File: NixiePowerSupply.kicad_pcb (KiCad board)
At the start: 2 copper layers, 22 parts, among them J1 BARREL_JACK, J2 CONN_01X04, J3 CONN_01X05, Q1 2SA1015, Q2 2SK3234, U1 NJM2360, U2 7805

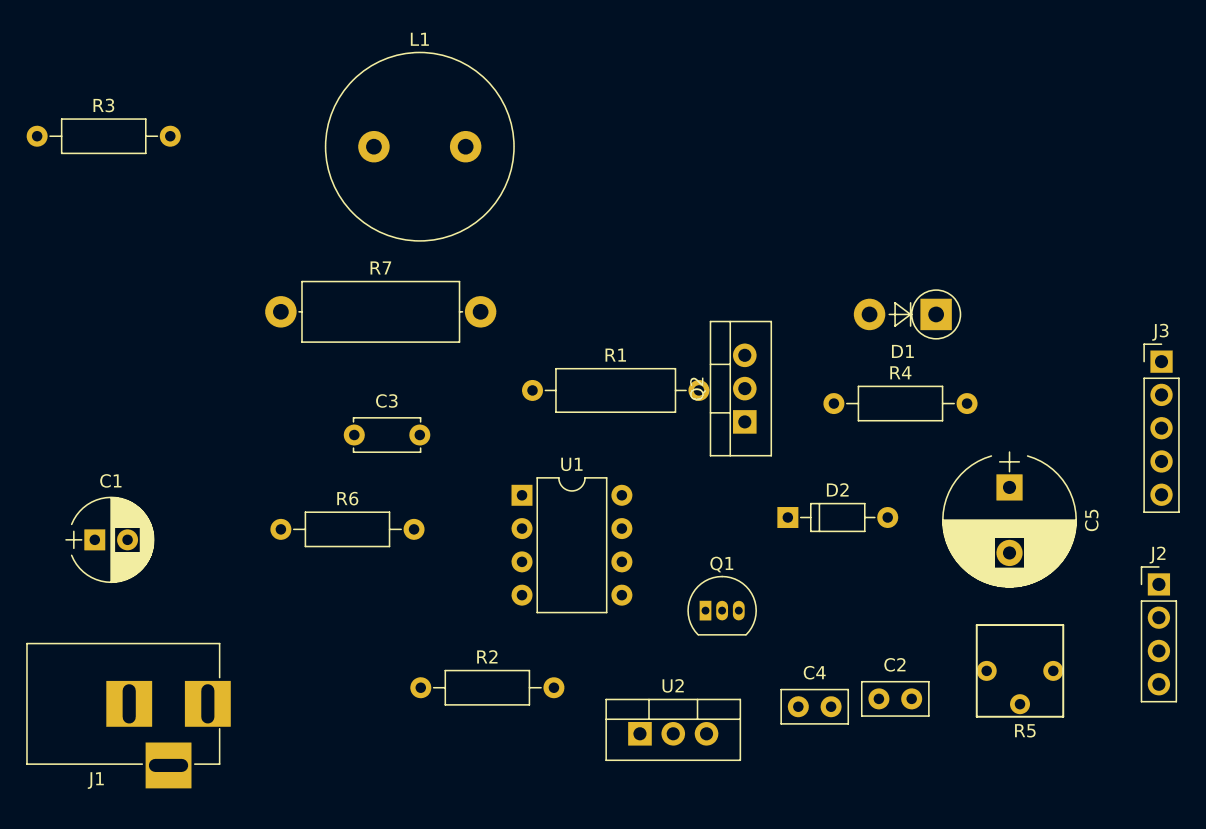
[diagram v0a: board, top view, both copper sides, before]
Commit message: parts moved for layout chnge
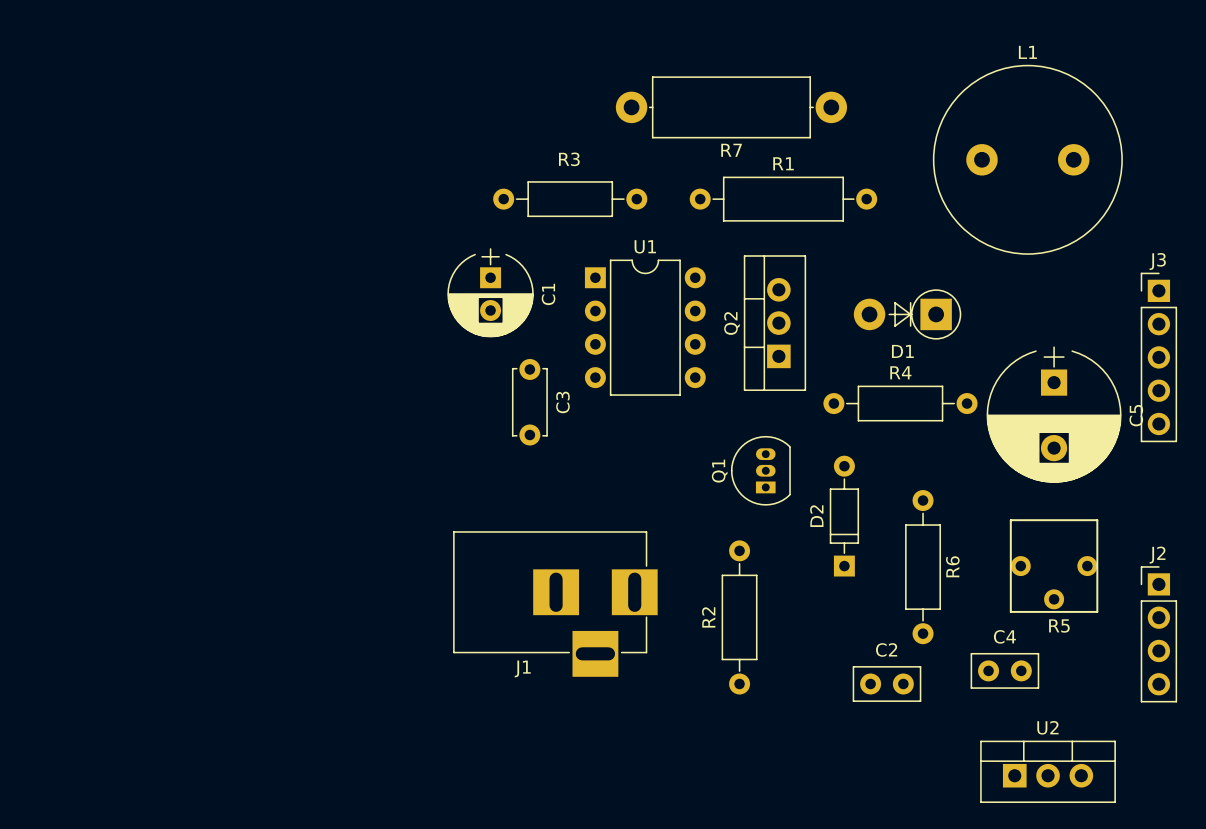
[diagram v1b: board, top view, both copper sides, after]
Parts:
- moved R6 49.0 mm to (206.0, 56.0), turned to 270 degrees
- moved L1 46.4 mm to (214.0, 30.0)
- moved R7 44.8 mm to (199.0, 26.0), turned to 180 degrees
- moved C1 36.2 mm to (173.0, 39.0), turned to 270 degrees
- moved R3 35.9 mm to (174.0, 33.0)
- moved J1 33.7 mm to (184.0, 63.0)
- moved U2 28.8 mm to (213.0, 77.0)
- moved R2 24.3 mm to (192.0, 70.0), turned to 90 degrees
- moved R1 19.4 mm to (189.0, 33.0)
- moved U1 17.5 mm to (181.0, 39.0)
- moved C4 14.8 mm to (211.0, 69.0)
- moved C3 14.3 mm to (176.0, 46.0), turned to 270 degrees
- moved Q1 10.5 mm to (194.0, 55.0), turned to 90 degrees
- moved C5 8.69 mm to (216.0, 47.0)
- moved R5 8.41 mm to (216.0, 61.0)
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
